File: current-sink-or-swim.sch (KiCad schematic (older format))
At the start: 12 parts

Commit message: Added voltage control and reorganized/cleaned up the page
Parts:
- removed U?: TC1016, symbol TC1016
- added C?: C, symbol C
- added D?: D, symbol D
- added J?: CONN_01X03_MALE, symbol CONN_01X03_MALE
- added J?: CONN_01X02_MALE, symbol CONN_01X02_MALE
- added R?: 27K, symbol R
- added R?: 21.6K, symbol R
- added R? (x2): 1K, symbol R
- added R?: R, symbol R
- added R?: 9K, symbol R
- added RV?: POT, symbol POT
- added U?: LM2931, symbol LM2931
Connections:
- net labels added: CURRENT_SINK+, GATE, VIN
- wire segments 29 -> 87
- no-connect marks 6 -> 2
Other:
- note added: "Battery Power"
- note added: "Current Control"
- note added: "Current Sink Input"
- note added: "Power Regulation"
- note added: "Selector"
- note added: "Voltage Control"
- moved on the sheet: C?, J?, Q?, R?, RV?, U?A, U?B

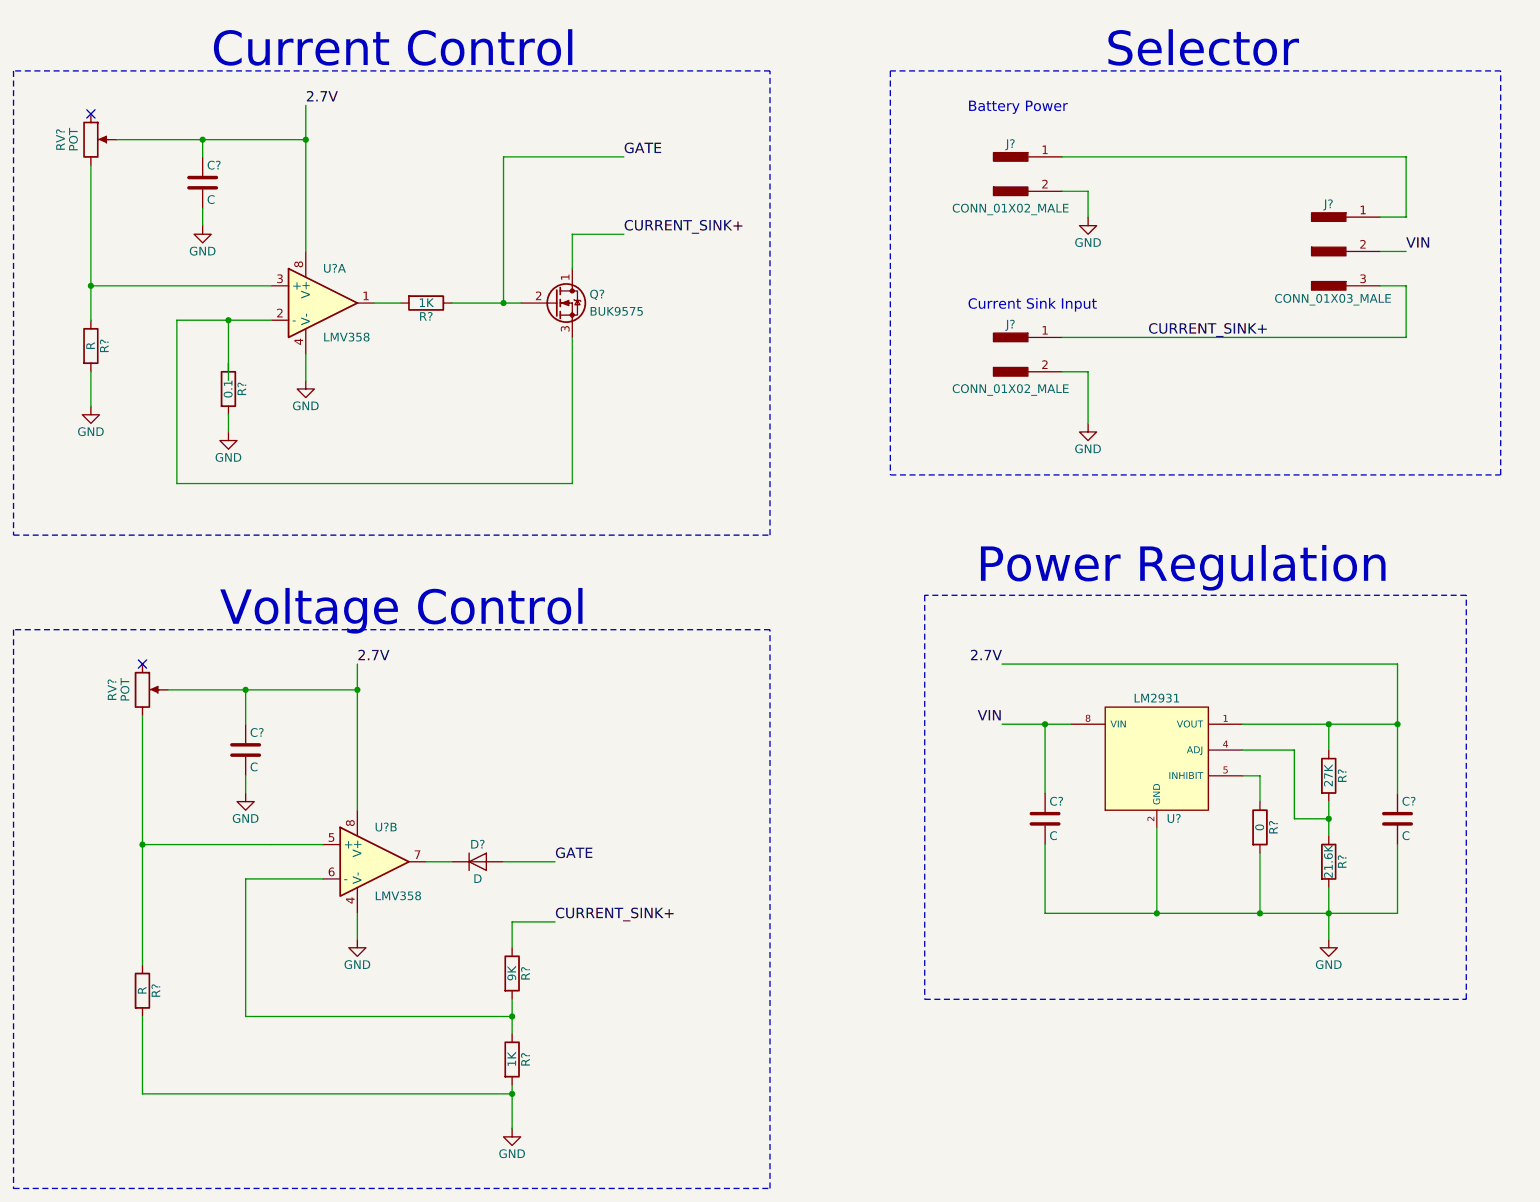
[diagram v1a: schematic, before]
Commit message: Annotated schematic automatically and then made some manual tweaks
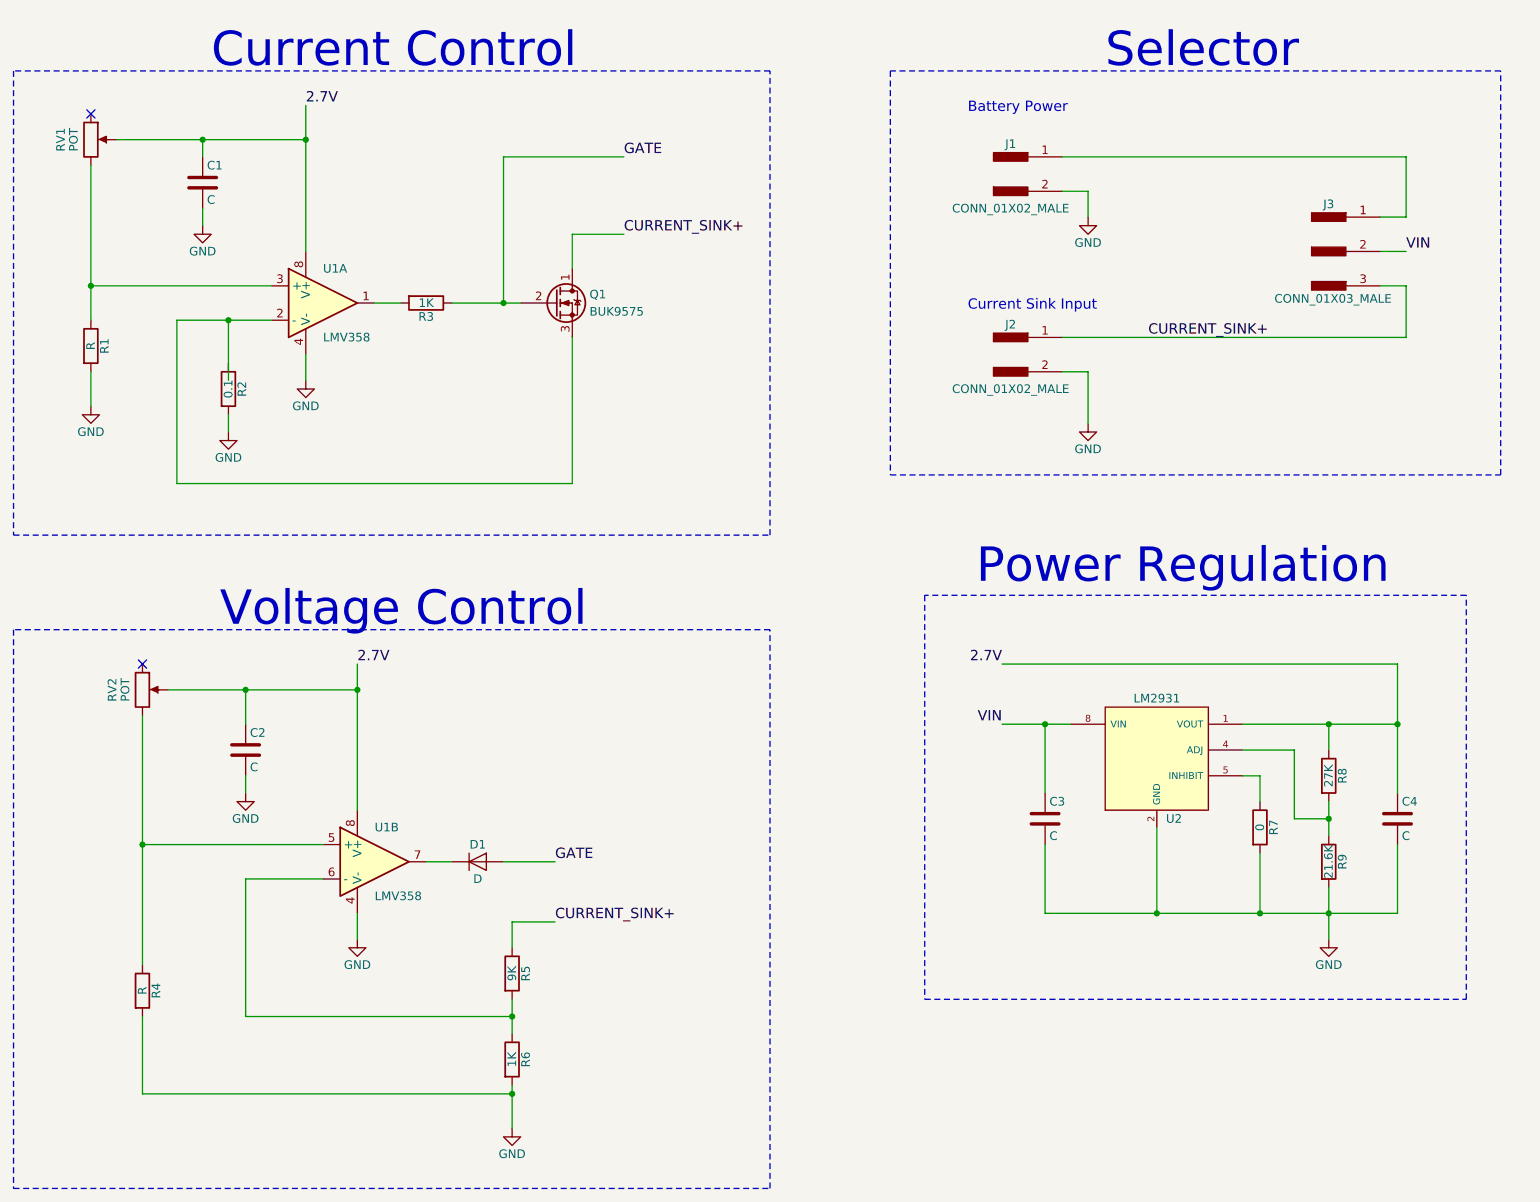
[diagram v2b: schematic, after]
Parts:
- gave numbers to parts that had none: 22
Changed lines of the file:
@@
 $EndDescr
 $Comp
-L LMV358 U?
+L LMV358 U1
 U 1 1 591E789A
 P 3100 2300
-F 0 "U?" H 3100 2500 50  0000 L CNN
+F 0 "U1" H 3100 2500 50  0000 L CNN
 F 1 "LMV358" H 3100 2100 50  0000 L CNN
 F 2 "" H 3100 2300 50  0001 C CNN
@@
 $EndComp
 $Comp
-L R R?
+L R R2
 U 1 1 591E78DF
 P 2550 2800
-F 0 "R?" V 2630 2800 50  0000 C CNN
+F 0 "R2" V 2630 2800 50  0000 C CNN
 F 1 "0.1" V 2550 2800 50  0000 C CNN
 F 2 "" V 2480 2800 50  0001 C CNN
@@
 $EndComp
 $Comp
-L GND #PWR?
+L GND #PWR3
 U 1 1 591E7948
 P 2550 3050
-F 0 "#PWR?" H 2550 2800 50  0001 C CNN
+F 0 "#PWR3" H 2550 2800 50  0001 C CNN
 F 1 "GND" H 2550 2900 50  0000 C CNN
 F 2 "" H 2550 3050 50  0001 C CNN
@@
 $EndComp
 $Comp
-L R R?
+L R R1
 U 1 1 591E7A1F
 P 1750 2550
-F 0 "R?" V 1830 2550 50  0000 C CNN
+F 0 "R1" V 1830 2550 50  0000 C CNN
 F 1 "R" V 1750 2550 50  0000 C CNN
 F 2 "" V 1680 2550 50  0001 C CNN
@@
 $EndComp
 $Comp
-L GND #PWR?
+L GND #PWR5
 U 1 1 591E7A85
 P 3000 2750
-F 0 "#PWR?" H 3000 2500 50  0001 C CNN
+F 0 "#PWR5" H 3000 2500 50  0001 C CNN
 F 1 "GND" H 3000 2600 50  0000 C CNN
 F 2 "" H 3000 2750 50  0001 C CNN
@@
 $EndComp
 $Comp
-L C C?
+L C C3
 U 1 1 591E7E69
 P 7300 5300
-F 0 "C?" H 7325 5400 50  0000 L CNN
+F 0 "C3" H 7325 5400 50  0000 L CNN
 F 1 "C" H 7325 5200 50  0000 L CNN
 F 2 "" H 7338 5150 50  0001 C CNN
@@
 $EndComp
 $Comp
-L C C?
+L C C4
 U 1 1 591E7EA0
 P 9350 5300
-F 0 "C?" H 9375 5400 50  0000 L CNN
+F 0 "C4" H 9375 5400 50  0000 L CNN
 F 1 "C" H 9375 5200 50  0000 L CNN
 F 2 "" H 9388 5150 50  0001 C CNN
@@
 $EndComp
 $Comp
-L CONN_01X02_MALE J?
+L CONN_01X02_MALE J2
 U 1 1 591E8ADC
 P 7100 2600
-F 0 "J?" H 7100 2775 50  0000 C CNN
+F 0 "J2" H 7100 2775 50  0000 C CNN
 F 1 "CONN_01X02_MALE" H 7100 2400 50  0000 C CNN
 F 2 "" H 7100 2700 50  0001 C CNN
@@
 $EndComp
 $Comp
-L Q_NMOS_DGS Q?
+L Q_NMOS_DGS Q1
 U 1 1 591E8B34
 P 4450 2300
-F 0 "Q?" H 4650 2350 50  0000 L CNN
+F 0 "Q1" H 4650 2350 50  0000 L CNN
 F 1 "BUK9575" H 4650 2250 50  0000 L CNN
 F 2 "" H 4650 2400 50  0001 C CNN
@@
 $EndComp
 $Comp
-L GND #PWR?
+L GND #PWR9
 U 1 1 591E8C41
 P 7550 3000
-F 0 "#PWR?" H 7550 2750 50  0001 C CNN
+F 0 "#PWR9" H 7550 2750 50  0001 C CNN
 F 1 "GND" H 7550 2850 50  0000 C CNN
 F 2 "" H 7550 3000 50  0001 C CNN
@@
 $EndComp
 $Comp
-L POT RV?
+L POT RV1
 U 1 1 591E8CD3
 P 1750 1350
-F 0 "RV?" V 1575 1350 50  0000 C CNN
+F 0 "RV1" V 1575 1350 50  0000 C CNN
 F 1 "POT" V 1650 1350 50  0000 C CNN
 F 2 "" H 1750 1350 50  0001 C CNN
@@
 $EndComp
 $Comp
-L LMV358 U?
+L LMV358 U1
 U 2 1 591E8E9A
 P 3400 5550
-F 0 "U?" H 3400 5750 50  0000 L CNN
+F 0 "U1" H 3400 5750 50  0000 L CNN
 F 1 "LMV358" H 3400 5350 50  0000 L CNN
 F 2 "" H 3400 5550 50  0001 C CNN
@@
 $EndComp
 $Comp
-L R R?
+L R R7
 U 1 1 591E98C6
 P 8550 5350
-F 0 "R?" V 8630 5350 50  0000 C CNN
+F 0 "R7" V 8630 5350 50  0000 C CNN
 F 1 "0" V 8550 5350 50  0000 C CNN
 F 2 "" V 8480 5350 50  0001 C CNN
@@
 $EndComp
 $Comp
-L C C?
+L C C1
 U 1 1 591E9A61
 P 2400 1600
-F 0 "C?" H 2425 1700 50  0000 L CNN
+F 0 "C1" H 2425 1700 50  0000 L CNN
 F 1 "C" H 2425 1500 50  0000 L CNN
 F 2 "" H 2438 1450 50  0001 C CNN
@@
 $EndComp
 $Comp
-L GND #PWR?
+L GND #PWR2
 U 1 1 591E9C9E
 P 2400 1850
-F 0 "#PWR?" H 2400 1600 50  0001 C CNN
+F 0 "#PWR2" H 2400 1600 50  0001 C CNN
 F 1 "GND" H 2400 1700 50  0000 C CNN
 F 2 "" H 2400 1850 50  0001 C CNN
@@
 $EndComp
 $Comp
-L LM2931 U?
+L LM2931 U2
 U 1 1 591F9C4D
 P 7950 4900
-F 0 "U?" H 8050 4500 50  0000 C CNN
+F 0 "U2" H 8050 4500 50  0000 C CNN
 F 1 "LM2931" H 7950 5200 50  0000 C CNN
 F 2 "" H 7950 4700 50  0001 C CNN
@@
 $EndComp
 $Comp
-L GND #PWR?
+L GND #PWR1
 U 1 1 591FB5E5
 P 1750 2900
-F 0 "#PWR?" H 1750 2650 50  0001 C CNN
+F 0 "#PWR1" H 1750 2650 50  0001 C CNN
 F 1 "GND" H 1750 2750 50  0000 C CNN
 F 2 "" H 1750 2900 50  0001 C CNN
@@
 $EndComp
 $Comp
-L R R?
+L R R8
 U 1 1 591FC13A
 P 8950 5050
-F 0 "R?" V 9030 5050 50  0000 C CNN
+F 0 "R8" V 9030 5050 50  0000 C CNN
 F 1 "27K" V 8950 5050 50  0000 C CNN
 F 2 "" V 8880 5050 50  0001 C CNN
@@
 $EndComp
 $Comp
-L R R?
+L R R9
 U 1 1 591FC19C
 P 8950 5550
-F 0 "R?" V 9030 5550 50  0000 C CNN
+F 0 "R9" V 9030 5550 50  0000 C CNN
 F 1 "21.6K" V 8950 5550 50  0000 C CNN
 F 2 "" V 8880 5550 50  0001 C CNN
@@
 $EndComp
 $Comp
-L GND #PWR?
+L GND #PWR10
 U 1 1 591FC2A9
 P 8950 6000
-F 0 "#PWR?" H 8950 5750 50  0001 C CNN
+F 0 "#PWR10" H 8950 5750 50  0001 C CNN
 F 1 "GND" H 8950 5850 50  0000 C CNN
 F 2 "" H 8950 6000 50  0001 C CNN
@@
 $EndComp
 $Comp
-L CONN_01X03_MALE J?
+L CONN_01X03_MALE J3
 U 1 1 59204531
 P 8950 2000
-F 0 "J?" H 8950 2275 50  0000 C CNN
+F 0 "J3" H 8950 2275 50  0000 C CNN
 F 1 "CONN_01X03_MALE" H 8975 1725 50  0000 C CNN
 F 2 "" H 8950 2200 50  0001 C CNN
@@
 $EndComp
 $Comp
-L CONN_01X02_MALE J?
+L CONN_01X02_MALE J1
 U 1 1 59205542
 P 7100 1550
-F 0 "J?" H 7100 1725 50  0000 C CNN
+F 0 "J1" H 7100 1725 50  0000 C CNN
 F 1 "CONN_01X02_MALE" H 7100 1350 50  0000 C CNN
 F 2 "" H 7100 1650 50  0001 C CNN
@@
 $EndComp
 $Comp
-L GND #PWR?
+L GND #PWR8
 U 1 1 592055FA
 P 7550 1800
-F 0 "#PWR?" H 7550 1550 50  0001 C CNN
+F 0 "#PWR8" H 7550 1550 50  0001 C CNN
 F 1 "GND" H 7550 1650 50  0000 C CNN
 F 2 "" H 7550 1800 50  0001 C CNN
@@
 $EndComp
 $Comp
-L D D?
+L D D1
 U 1 1 59207359
 P 4000 5550
-F 0 "D?" H 4000 5650 50  0000 C CNN
+F 0 "D1" H 4000 5650 50  0000 C CNN
 F 1 "D" H 4000 5450 50  0000 C CNN
 F 2 "" H 4000 5550 50  0001 C CNN
@@
 $EndComp
 $Comp
-L R R?
+L R R3
 U 1 1 5920824C
 P 3700 2300
-F 0 "R?" V 3780 2300 50  0000 C CNN
+F 0 "R3" V 3780 2300 50  0000 C CNN
 F 1 "1K" V 3700 2300 50  0000 C CNN
 F 2 "" V 3630 2300 50  0001 C CNN
@@
 $EndComp
 $Comp
-L R R?
+L R R4
 U 1 1 592089E3
 P 2050 6300
-F 0 "R?" V 2130 6300 50  0000 C CNN
+F 0 "R4" V 2130 6300 50  0000 C CNN
 F 1 "R" V 2050 6300 50  0000 C CNN
 F 2 "" V 1980 6300 50  0001 C CNN
@@
 $EndComp
 $Comp
-L POT RV?
+L POT RV2
 U 1 1 59208E84
 P 2050 4550
-F 0 "RV?" V 1875 4550 50  0000 C CNN
+F 0 "RV2" V 1875 4550 50  0000 C CNN
 F 1 "POT" V 1950 4550 50  0000 C CNN
 F 2 "" H 2050 4550 50  0001 C CNN
@@
 $EndComp
 $Comp
-L C C?
+L C C2
 U 1 1 5920A143
 P 2650 4900
-F 0 "C?" H 2675 5000 50  0000 L CNN
+F 0 "C2" H 2675 5000 50  0000 L CNN
 F 1 "C" H 2675 4800 50  0000 L CNN
 F 2 "" H 2688 4750 50  0001 C CNN
@@
 $EndComp
 $Comp
-L GND #PWR?
+L GND #PWR4
 U 1 1 5920ABD4
 P 2650 5150
-F 0 "#PWR?" H 2650 4900 50  0001 C CNN
+F 0 "#PWR4" H 2650 4900 50  0001 C CNN
 F 1 "GND" H 2650 5000 50  0000 C CNN
 F 2 "" H 2650 5150 50  0001 C CNN
@@
 $EndComp
 $Comp
-L R R?
+L R R6
 U 1 1 5920AFE7
 P 4200 6700
-F 0 "R?" V 4280 6700 50  0000 C CNN
+F 0 "R6" V 4280 6700 50  0000 C CNN
 F 1 "1K" V 4200 6700 50  0000 C CNN
 F 2 "" V 4130 6700 50  0001 C CNN
@@
 $EndComp
 $Comp
-L R R?
+L R R5
 U 1 1 5920B26E
 P 4200 6200
-F 0 "R?" V 4280 6200 50  0000 C CNN
+F 0 "R5" V 4280 6200 50  0000 C CNN
 F 1 "9K" V 4200 6200 50  0000 C CNN
 F 2 "" V 4130 6200 50  0001 C CNN
@@
 2.7V
 $Comp
-L GND #PWR?
+L GND #PWR7
 U 1 1 5920F8C3
 P 4200 7100
-F 0 "#PWR?" H 4200 6850 50  0001 C CNN
+F 0 "#PWR7" H 4200 6850 50  0001 C CNN
 F 1 "GND" H 4200 6950 50  0000 C CNN
 F 2 "" H 4200 7100 50  0001 C CNN
@@
 Power Regulation
 $Comp
-L GND #PWR?
+L GND #PWR6
 U 1 1 59216A4D
 P 3300 6000
-F 0 "#PWR?" H 3300 5750 50  0001 C CNN
+F 0 "#PWR6" H 3300 5750 50  0001 C CNN
 F 1 "GND" H 3300 5850 50  0000 C CNN
 F 2 "" H 3300 6000 50  0001 C CNN

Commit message: Added metadata for components and links to datasheets
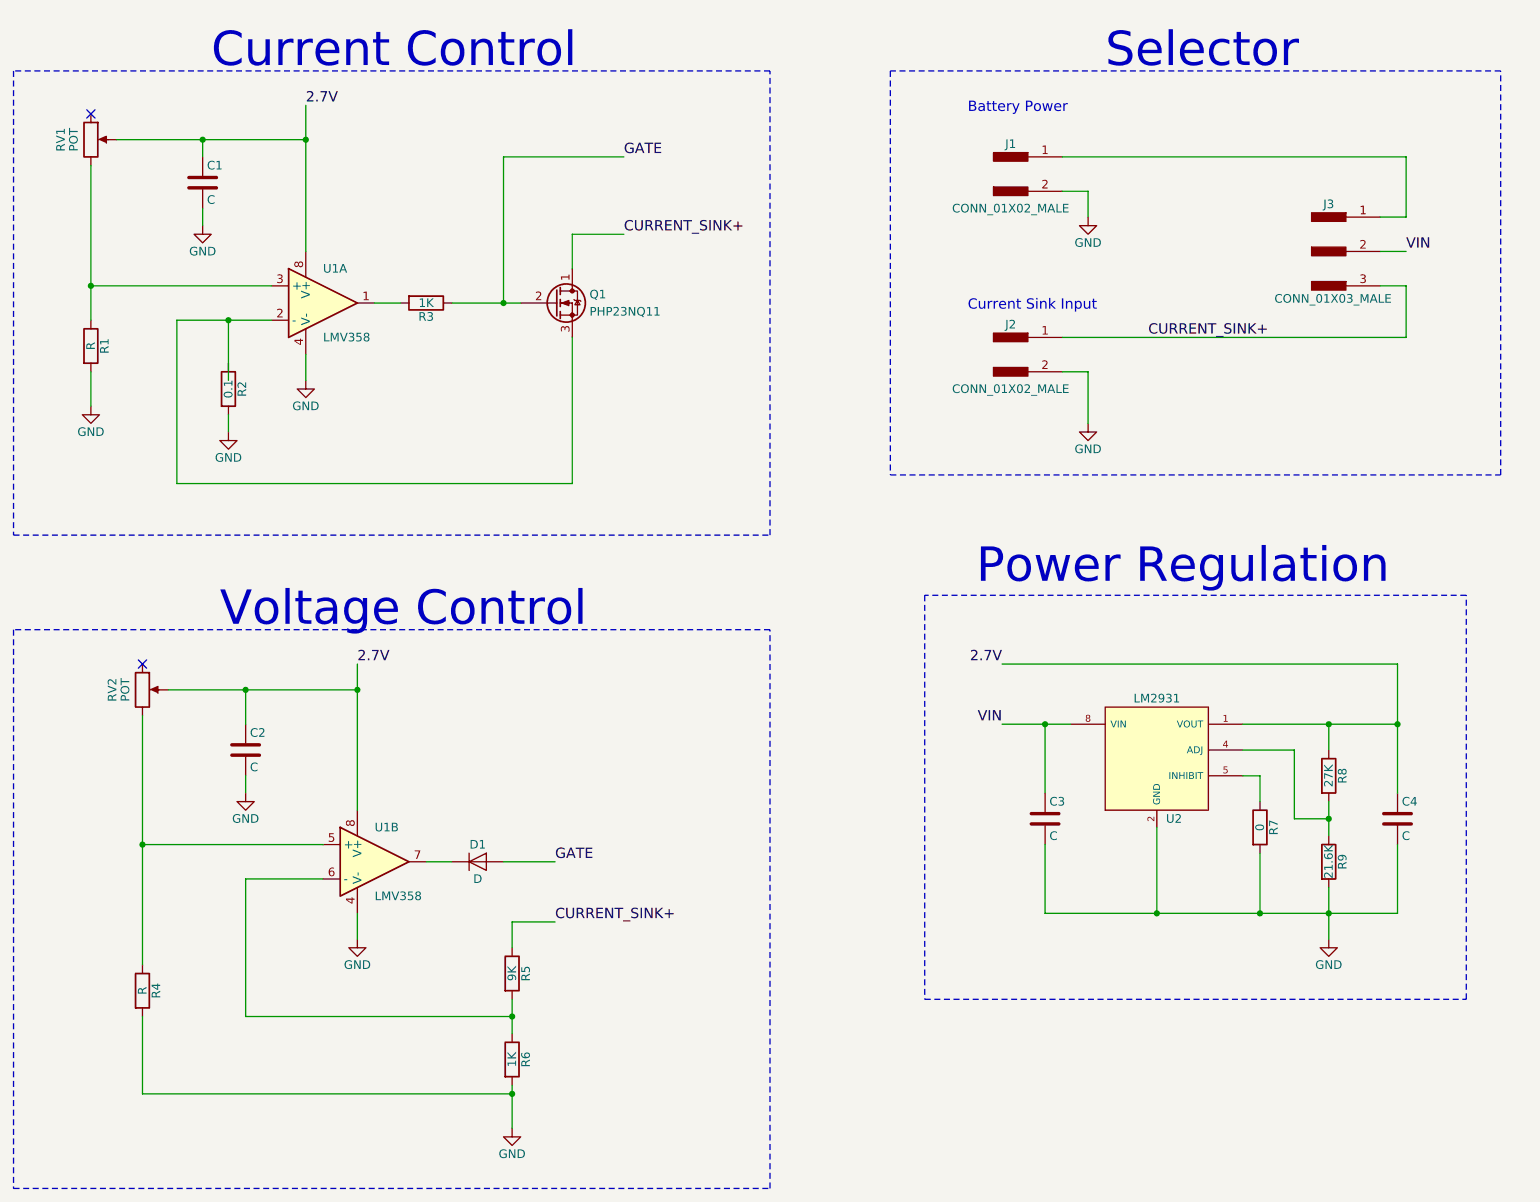
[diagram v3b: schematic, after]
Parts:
- C1, C2, C3, C4: footprint (none) -> Capacitors_SMD:C_0805_HandSoldering
- D1: footprint (none) -> Diodes_SMD:D_SOD-123; DKPN (none) -> 1N4148WTPMSCT-ND; MPN (none) -> 1N4148W-TP
- J1, J2: footprint (none) -> Pin_Headers:Pin_Header_Straight_1x02_Pitch2.54mm
- J3: footprint (none) -> Pin_Headers:Pin_Header_Straight_1x03_Pitch2.54mm
- Q1: value BUK9575 -> PHP23NQ11; footprint (none) -> TO_SOT_Packages_THT:TO-220_Vertical; DKPN (none) -> 1727-4642-ND; MPN BUK9575-100A,127 -> PHP23NQ11T,127
- R1, R3, R4, R5, R6, R7, R8, R9: footprint (none) -> Resistors_SMD:R_0805_HandSoldering
- R2: footprint (none) -> Resistors_THT:R_Axial_DIN0414_L11.9mm_D4.5mm_P15.24mm_Horizontal; DKPN (none) -> PPC1W.10CT-ND
- RV1, RV2: footprint (none) -> Potentiometers:Potentiometer_Piher_PC-16_Single_Horizontal
- U1: footprint (none) -> Housings_SOIC:SOIC-8_3.9x4.9mm_Pitch1.27mm
- U1: footprint (none) -> Housings_SOIC:SOIC-8_3.9x4.9mm_Pitch1.27mm; DKPN (none) -> 497-4945-1-ND; MPN (none) -> LMV358IDT
- U2: footprint (none) -> Housings_SOIC:SOIC-8_3.9x4.9mm_Pitch1.27mm; DKPN (none) -> LM2931CDR2GOSCT-ND; MPN (none) -> LM2931CDR2G

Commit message: Added heatsink and updated to correct FET symbol
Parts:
- removed C1: C, Capacitors_SMD:C_0805_HandSoldering, symbol C
- added HEATSINK1: HEATSINK, Heatsinks:FA-T220-25E_42x25mm_2xDrill2.5mm, symbol CONN_01X01
- C2, C3, C4: value C -> 0.1
- J1, J2: footprint Pin_Headers:Pin_Header_Straight_1x02_Pitch2.54mm -> CSOS Connectors:TerminalBlock_Pheonix_PT-5mm_2pol; DKPN (none) -> 277-2518-ND; MPN (none) -> 1792863
- Q1: symbol Q_NMOS_DGS -> Q_NJFET_GDS
- R1: value R -> 68K
- R4: value R -> 28.7K
- RV1, RV2: value POT -> 10K; footprint Potentiometers:Potentiometer_Piher_PC-16_Single_Horizontal -> CSOS Passives:P090L-02F25BR10K
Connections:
- net 2.7V: now also R1.1, R4.1; no longer RV1.2, RV2.2
- net CURRENT_SINK+: now also Q1.2 (D); no longer Q1.1 (D)
- net GND: now also RV1.3, RV2.3; no longer R1.2, R4.2
- net at U1.1: now also D1.1 (K); no longer R3.2
- net at U1.2 (-): now also R5.2, R6.1; no longer Q1.3 (S)
- net at R2.1: now also Q1.3 (S), U1.6 (-)
- net at U1.7: now also R3.2; no longer D1.1 (K)
- net GATE renamed VCONTROL
- net VCONTROL: now also Q1.1 (G); no longer Q1.2 (G)
- new net: R4.2, RV2.2, U1.3 (+)
- new net: R1.2, RV1.2, U1.5 (+)
- no-connect marks 2 -> 3
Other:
- note added: "0-20V"
- note added: "0-2V"
- moved on the sheet: R1, R2, R4, RV1, RV2, U1A, U1B
